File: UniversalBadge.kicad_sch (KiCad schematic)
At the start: 18 parts, among them J1 Conn_01x03_Pin, J2 Conn_01x05_Pin, J3 Conn_02x04_Counter_Clockwise, SW1 Push_Button, U1 ATTINY85-20PU

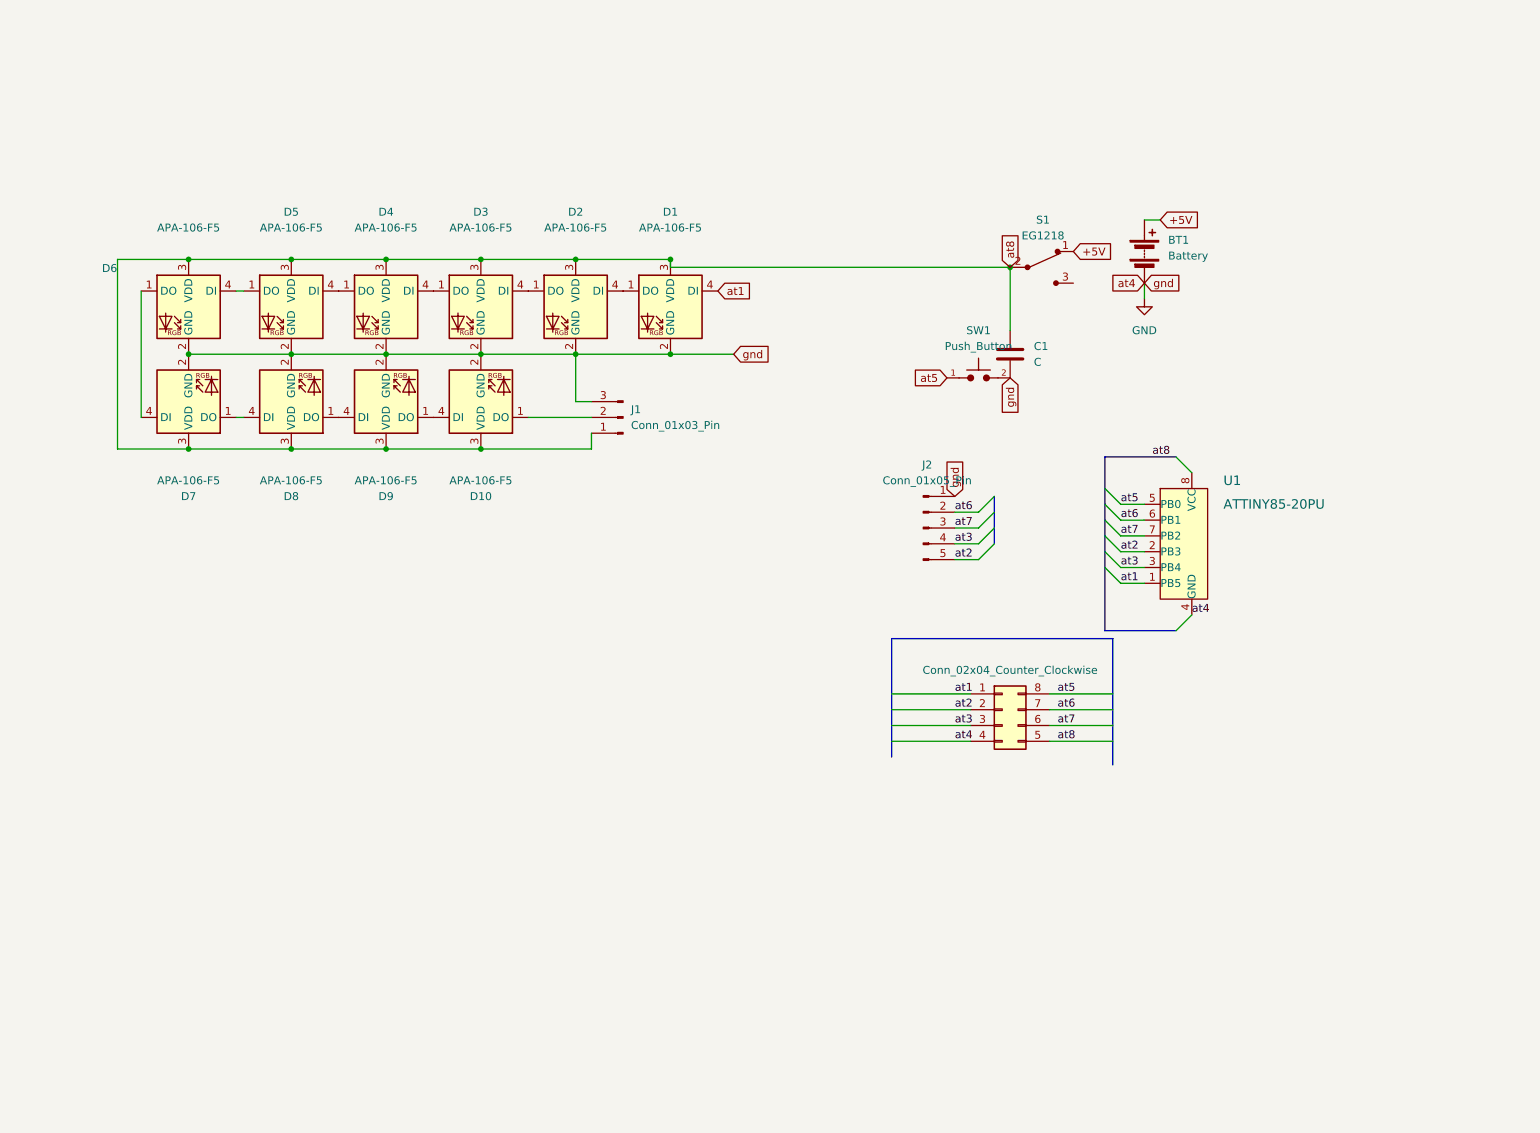
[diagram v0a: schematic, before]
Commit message: redo board layout
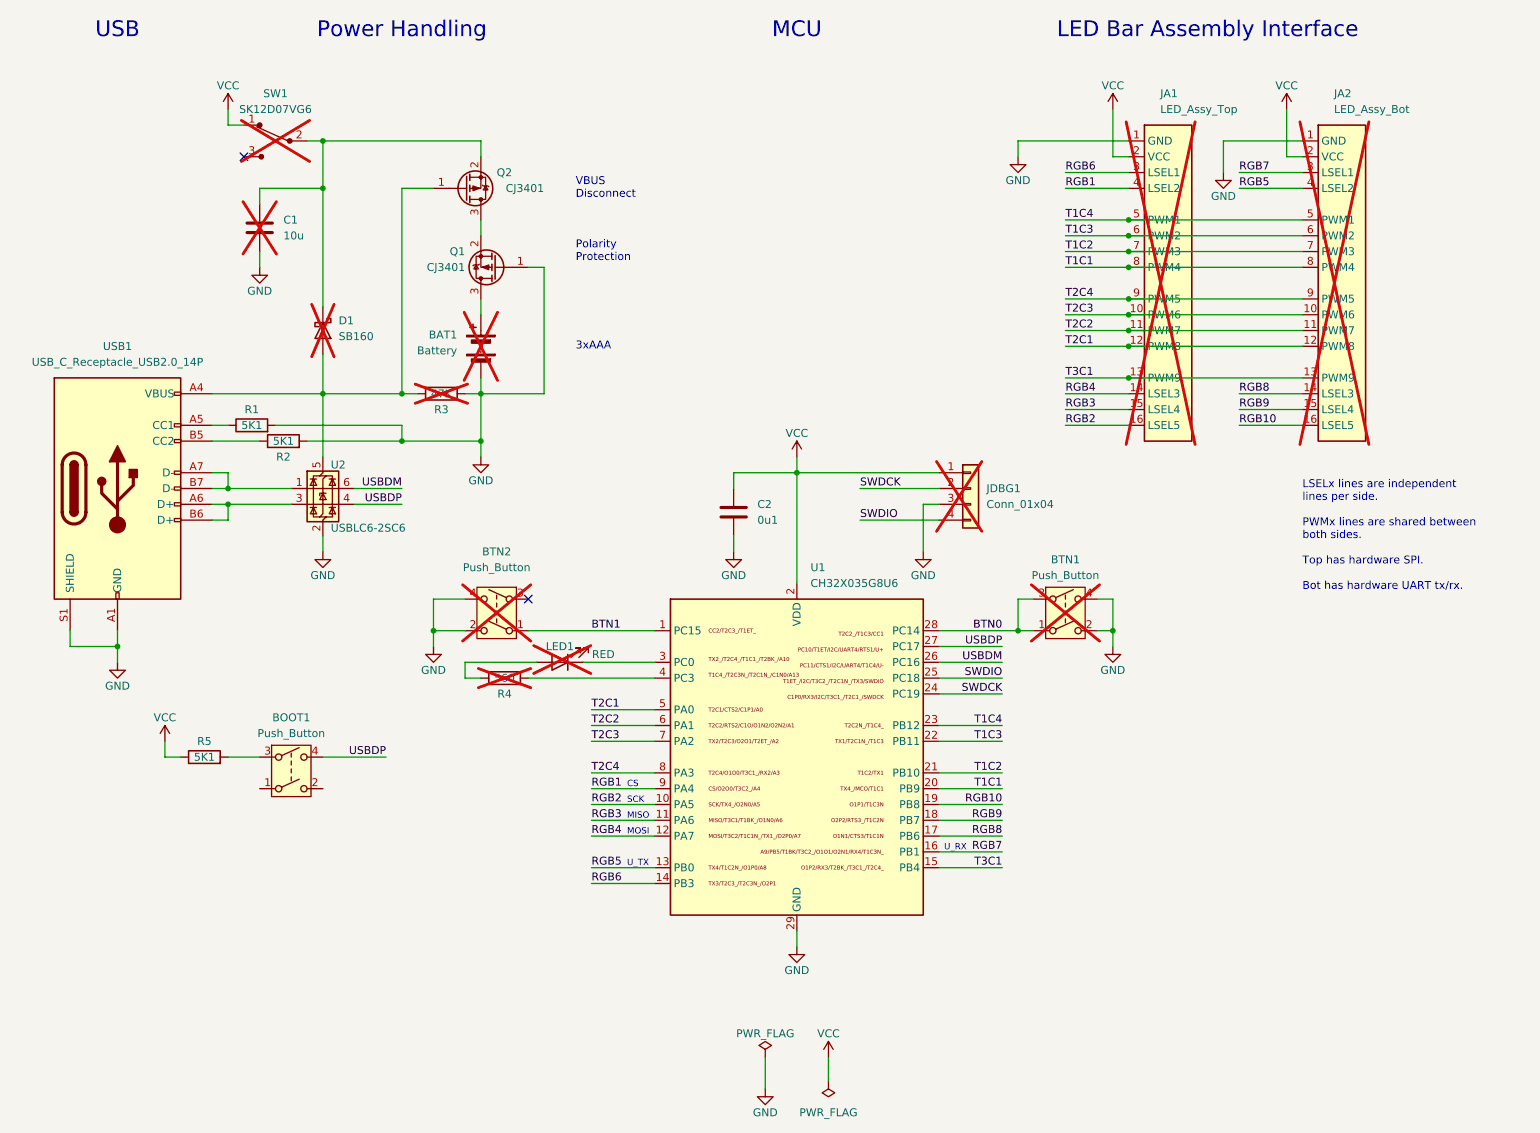
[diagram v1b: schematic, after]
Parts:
- removed BT1: Battery, Battery:BatteryHolder_ComfortableElectronic_CH273-2450_1x2450, symbol Device:Battery
- removed D1, D10, D2, D3, D4, D5, D6, D7, D8, D9: APA-106-F5, LED_THT:LED_D5.0mm-4_RGB, symbol LED:APA-106-F5
- removed J1: Conn_01x03_Pin, Connector_PinHeader_2.54mm:PinHeader_1x03_P2.54mm_Vertical, symbol Connector:Conn_01x03_Pin
- removed J2: Conn_01x05_Pin, Connector_PinHeader_2.54mm:PinHeader_1x05_P2.54mm_Vertical, symbol Connector:Conn_01x05_Pin
- removed J3: Conn_02x04_Counter_Clockwise, Connector_PinHeader_2.54mm:PinHeader_2x04_P2.54mm_Vertical, symbol Connector_Generic:Conn_02x04_Counter_Clockwise
- removed S1: EG1218, digikey-footprints:Switch_Slide_11.6x4mm_EG1218, symbol dk_Slide-Switches:EG1218
- removed SW1: Push_Button, Button_Switch_THT:SW_PUSH_6mm, symbol PCM_SL_Devices:Push_Button
- removed U1: ATTINY85-20PU, digikey-footprints:DIP-8_W7.62mm, symbol dk_Embedded-Microcontrollers:ATTINY85-20PU
- added BAT1: Battery, _trueControl:MYOUNG BH-AAA-Axxx024, symbol Device:Battery
- added BOOT1: Push_Button, _trueControl:TactSw_Hanbo_TS-KG057S-BT34F, symbol Switch:SW_DPST
- added BTN1, BTN2: Push_Button, Button_Switch_THT:SW_PUSH_6mm, symbol Switch:SW_DPST
- added C2: 0u1, Capacitor_SMD:C_0603_1608Metric_Pad1.08x0.95mm_HandSolder, symbol Device:C
- added D1: SB160, Diode_THT:D_DO-41_SOD81_P10.16mm_Horizontal, symbol Device:D_Schottky
- added JA1: LED_Assy_Top, _trueControl:Stacking_Module_16P_REV2, symbol _trueControl:LED_Assy
- added JA2: LED_Assy_Bot, _trueControl:Stacking_Module_16P_REV2, symbol _trueControl:LED_Assy
- added JDBG1: Conn_01x04, Connector_PinHeader_2.54mm:PinHeader_1x04_P2.54mm_Vertical, symbol Connector_Generic:Conn_01x04
- added LED1: RED, LED_THT:LED_D3.0mm, symbol Device:LED
- added Q1, Q2: CJ3401, Package_TO_SOT_SMD:SOT-23, symbol Transistor_FET:IRLML9301
- added R1, R2, R5: 5K1, Resistor_SMD:R_0603_1608Metric_Pad0.98x0.95mm_HandSolder, symbol Device:R
- added R3: 47K, Resistor_THT:R_Axial_DIN0204_L3.6mm_D1.6mm_P7.62mm_Horizontal, symbol Device:R
- added R4: 560, Resistor_THT:R_Axial_DIN0204_L3.6mm_D1.6mm_P7.62mm_Horizontal, symbol Device:R
- added SW1: SK12D07VG6, Button_Switch_THT:SW_Slide_SPDT_Angled_CK_OS102011MA1Q, symbol dk_Slide-Switches:EG1218
- added U1: CH32X035G8U6, _trueControl:QFN-28-1EP_4x4mm_P0.4mm_EP2.4x2.4mm_ThermalVias_LP, symbol _trueControl:CH32X035G8U6
- added U2: USBLC6-2SC6, Package_TO_SOT_SMD:SOT-23-6, symbol Power_Protection:USBLC6-2SC6
- added USB1: USB_C_Receptacle_USB2.0_14P, Connector_USB:USB_C_Receptacle_HRO_TYPE-C-31-M-12, symbol Connector:USB_C_Receptacle_USB2.0_14P
- C1: value C -> 10u; footprint Capacitor_THT:C_Radial_D5.0mm_H5.0mm_P2.00mm -> Capacitor_THT:C_Disc_D6.0mm_W4.4mm_P5.00mm; LCSC (none) -> C2761733; now not fitted
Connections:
- net at8 is gone; now on net GND: C1.1
- net GND: now also BAT1.2 (-), BTN1.2, BTN1.4, BTN2.2, BTN2.4, C2.1, JA1.1 (GND), JA2.1 (GND), JDBG1.3 (Pin_3), Q1.1 (G), R1.2, R2.2, R3.1, U1.29 (GND), U2.2 (GND), USB1.A1 (GND), USB1.A12 (GND), USB1.B1 (GND), USB1.B12 (GND), USB1.S1 (SHIELD); no longer C1.2
- new net: Q1.2 (S), Q2.3 (D)
- new net: BAT1.1 (+), Q1.3 (D)
- new net: BOOT1.3, R5.2
- new net: D1.2 (A), Q2.1 (G), R3.2, U2.5 (VBUS), USB1.A4 (VBUS), USB1.A9 (VBUS), USB1.B4 (VBUS), USB1.B9 (VBUS)
- new net: R1.1, USB1.A5 (CC1)
- new net: U2.3 (I/O2), USB1.A6 (D+), USB1.B6 (D+)
- new net: U2.1 (I/O1), USB1.A7 (D-), USB1.B7 (D-)
- new net: R2.1, USB1.B5 (CC2)
- new net: C1.2, D1.1 (K), Q2.2 (S), SW1.2
- new net: LED1.1 (K), U1.3 (PC0)
- new net: LED1.2 (A), R4.1
- new net: R4.2, U1.4 (PC3)
- new net BTN0: BTN1.1, BTN1.3, U1.28 (PC14)
- new net BTN1: BTN2.1, U1.1 (PC15)
- new net RGB1: JA1.4 (LSEL2), U1.9 (PA4)
- new net RGB10: JA2.16 (LSEL5), U1.19 (PB8)
- new net RGB2: JA1.16 (LSEL5), U1.10 (PA5)
- new net RGB3: JA1.15 (LSEL4), U1.11 (PA6)
- new net RGB4: JA1.14 (LSEL3), U1.12 (PA7)
- new net RGB5: JA2.4 (LSEL2), U1.13 (PB0)
- new net RGB6: JA1.3 (LSEL1), U1.14 (PB3)
- new net RGB7: JA2.3 (LSEL1), U1.16 (PB1)
- new net RGB8: JA2.14 (LSEL3), U1.17 (PB6)
- new net RGB9: JA2.15 (LSEL4), U1.18 (PB7)
- new net SWDCK: JDBG1.2 (Pin_2), U1.24 (PC19)
- new net SWDIO: JDBG1.4 (Pin_4), U1.25 (PC18)
- new net T1C1: JA1.8 (PWM4), JA2.8 (PWM4), U1.20 (PB9)
- new net T1C2: JA1.7 (PWM3), JA2.7 (PWM3), U1.21 (PB10)
- new net T1C3: JA1.6 (PWM2), JA2.6 (PWM2), U1.22 (PB11)
- new net T1C4: JA1.5 (PWM1), JA2.5 (PWM1), U1.23 (PB12)
- new net T2C1: JA1.12 (PWM8), JA2.12 (PWM8), U1.5 (PA0)
- new net T2C2: JA1.11 (PWM7), JA2.11 (PWM7), U1.6 (PA1)
- new net T2C3: JA1.10 (PWM6), JA2.10 (PWM6), U1.7 (PA2)
- new net T2C4: JA1.9 (PWM5), JA2.9 (PWM5), U1.8 (PA3)
- new net T3C1: JA1.13 (PWM9), JA2.13 (PWM9), U1.15 (PB4)
- new net USBDM: U1.26 (PC16), U2.6 (I/O1)
- new net USBDP: BOOT1.4, U1.27 (PC17), U2.4 (I/O2)
- new net VCC: C2.2, JA1.2 (VCC), JA2.2 (VCC), JDBG1.1 (Pin_1), R5.1, SW1.1, U1.2 (VDD)
- no-connect marks 0 -> 2
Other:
- note added: "3xAAA"
- note added: "CS"
- note added: "LED Bar Assembly Interface"
- note added: "LSELx lines are independent lines per side. PWMx lines are shared between both sides. Top has hardware SPI. Bot has hardware UART tx/rx."
- note added: "MCU"
- note added: "MISO"
- note added: "MOSI"
- note added: "Polarity Protection"
- note added: "Power Handling"
- note added: "SCK"
- note added: "USB"
- note added: "U_RX"
- note added: "U_TX"
- note added: "VBUS Disconnect"
